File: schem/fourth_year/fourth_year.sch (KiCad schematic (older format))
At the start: 108 parts, among them P1 F Type, P10 BNC, P11 CONNECTOR, P12 CONNECTOR, P2 SAW, P3 CONNECTOR, P4 DC JACK, P5 CONNECTOR, P6 CONN_6, P7 CONN_1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

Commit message: More PCB work
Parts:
- removed P7: CONN_1, THROUGH HOLE CONN, symbol CONN_1
- removed P8: CONN_1, ~, symbol CONN_1
- added C54, C55, C56: 3uF, ~, symbol C
- added P7: BNC, ~, symbol BNC
- added T2: TRANSFO4, ~, symbol TRANSFO4
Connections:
- wire segments 441 -> 460
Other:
- note added: "I've put the + signal into the - input\nfor board routing convenience."

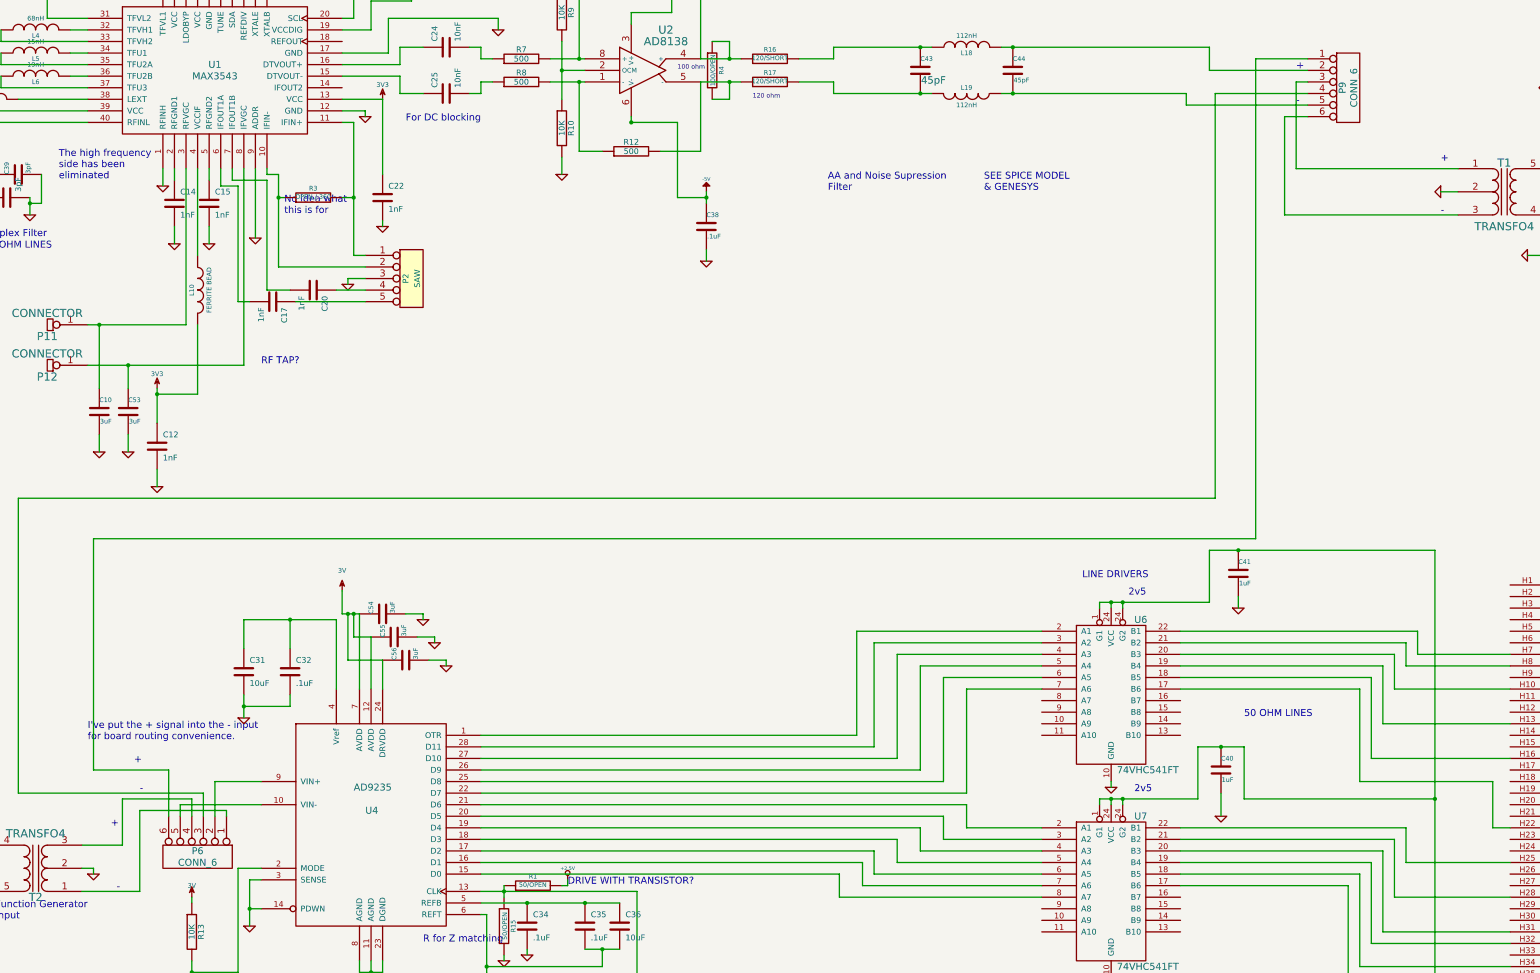
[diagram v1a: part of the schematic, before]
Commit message: Started routing ADC
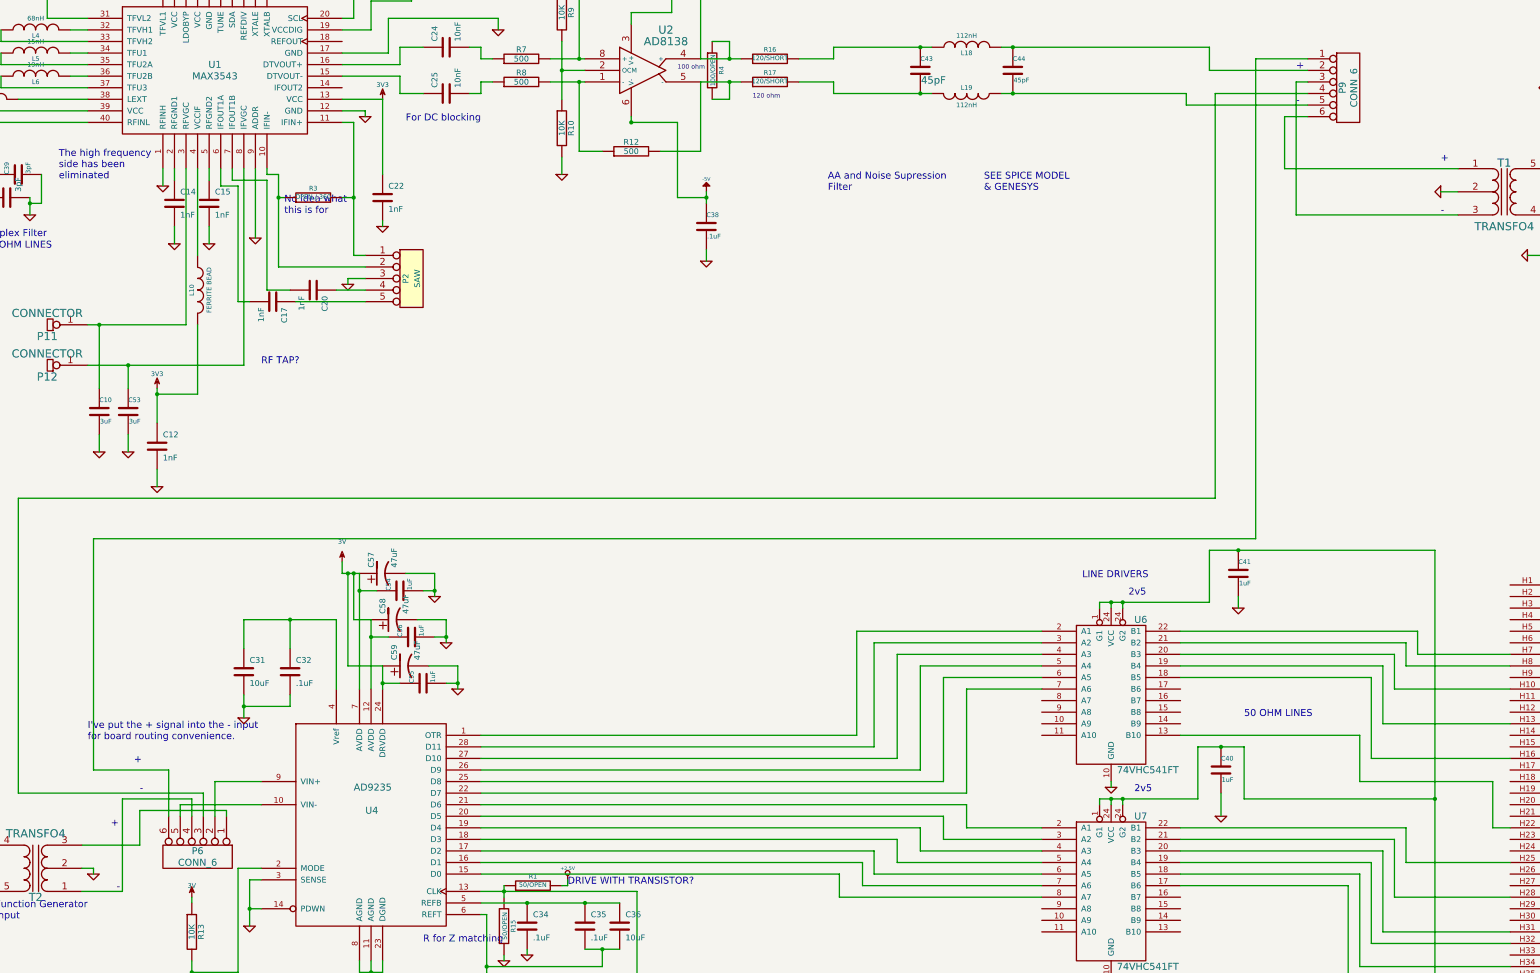
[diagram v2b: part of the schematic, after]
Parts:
- added C57, C58, C59: 47uF, ~, symbol CP1
- C54, C55, C56: value 3uF -> 1uF
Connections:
- wire segments 460 -> 466
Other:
- moved on the sheet: C54, C55, C56
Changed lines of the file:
@@
 Sheet 1 1
 Title ""
-Date "8 jan 2015"
+Date "9 jan 2015"
 Rev ""
 Comp ""
@@
 L 3V #PWR013
 U 1 1 54847F25
-P 4750 9850
-F 0 "#PWR013" H 4750 9950 40  0001 C CNN
-F 1 "3V" H 4750 10025 40  0000 C CNN
-F 2 "" H 4750 9850 60  0001 C CNN
-F 3 "" H 4750 9850 60  0001 C CNN
-	1    4750 9850
+P 4750 9600
+F 0 "#PWR013" H 4750 9700 40  0001 C CNN
+F 1 "3V" H 4750 9775 40  0000 C CNN
+F 2 "" H 4750 9600 60  0001 C CNN
+F 3 "" H 4750 9600 60  0001 C CNN
+	1    4750 9600
 	1    0    0    -1
 $EndComp
@@
 L C C55
 U 1 1 54AF12A6
-P 5200 10250
-F 0 "C55" H 5200 10350 40  0000 L CNN
-F 1 "3uF" H 5206 10165 40  0000 L CNN
-F 2 "~" H 5238 10100 30  0000 C CNN
-F 3 "~" H 5200 10250 60  0000 C CNN
-	1    5200 10250
+P 5450 10650
+F 0 "C55" H 5450 10750 40  0000 L CNN
+F 1 "1uF" H 5456 10565 40  0000 L CNN
+F 2 "~" H 5488 10500 30  0000 C CNN
+F 3 "~" H 5450 10650 60  0000 C CNN
+	1    5450 10650
 	0    -1   -1   0
 $EndComp
@@
 L C C54
 U 1 1 54AF12B5
-P 5100 10050
-F 0 "C54" H 5100 10150 40  0000 L CNN
-F 1 "3uF" H 5106 9965 40  0000 L CNN
-F 2 "~" H 5138 9900 30  0000 C CNN
-F 3 "~" H 5100 10050 60  0000 C CNN
-	1    5100 10050
+P 5250 9850
+F 0 "C54" H 5250 9950 40  0000 L CNN
+F 1 "1uF" H 5256 9765 40  0000 L CNN
+F 2 "~" H 5288 9700 30  0000 C CNN
+F 3 "~" H 5250 9850 60  0000 C CNN
+	1    5250 9850
 	0    -1   -1   0
 $EndComp
@@
 L C C56
 U 1 1 54AF258D
-P 5300 10450
-F 0 "C56" H 5300 10550 40  0000 L CNN
-F 1 "3uF" H 5306 10365 40  0000 L CNN
-F 2 "~" H 5338 10300 30  0000 C CNN
-F 3 "~" H 5300 10450 60  0000 C CNN
-	1    5300 10450
+P 5350 10250
+F 0 "C56" H 5350 10350 40  0000 L CNN
+F 1 "1uF" H 5356 10165 40  0000 L CNN
+F 2 "~" H 5388 10100 30  0000 C CNN
+F 3 "~" H 5350 10250 60  0000 C CNN
+	1    5350 10250
 	0    -1   -1   0
 $EndComp
+Text Notes 2550 11150 0    60   ~ 0
+I've put the + signal into the - input\nfor board routing convenience.
+$Comp
+L CP1 C58
+U 1 1 54B05B86
+P 5200 10100
+F 0 "C58" H 5250 10200 50  0000 L CNN
+F 1 "47uF" H 5250 10000 50  0000 L CNN
+F 2 "~" H 5200 10100 60  0000 C CNN
+F 3 "~" H 5200 10100 60  0000 C CNN
+	1    5200 10100
+	0    -1   -1   0
+$EndComp
+$Comp
+L CP1 C57
+U 1 1 54B05B93
+P 5100 9700
+F 0 "C57" H 5150 9800 50  0000 L CNN
+F 1 "47uF" H 5150 9600 50  0000 L CNN
+F 2 "~" H 5100 9700 60  0000 C CNN
+F 3 "~" H 5100 9700 60  0000 C CNN
+	1    5100 9700
+	0    -1   -1   0
+$EndComp
+$Comp
+L CP1 C59
+U 1 1 54B05B99
+P 5300 10500
+F 0 "C59" H 5350 10600 50  0000 L CNN
+F 1 "47uF" H 5350 10400 50  0000 L CNN
+F 2 "~" H 5300 10500 60  0000 C CNN
+F 3 "~" H 5300 10500 60  0000 C CNN
+	1    5300 10500
+	0    -1   -1   0
+$EndComp
+$Comp
+L GND #PWR086
+U 1 1 54B0765F
+P 5750 10700
+F 0 "#PWR086" H 5750 10700 30  0001 C CNN
+F 1 "GND" H 5750 10630 30  0001 C CNN
+F 2 "" H 5750 10700 60  0000 C CNN
+F 3 "" H 5750 10700 60  0000 C CNN
+	1    5750 10700
+	1    0    0    -1
+$EndComp
+$Comp
+L GND #PWR087
+U 1 1 54B0766C
+P 5650 10300
+F 0 "#PWR087" H 5650 10300 30  0001 C CNN
+F 1 "GND" H 5650 10230 30  0001 C CNN
+F 2 "" H 5650 10300 60  0000 C CNN
+F 3 "" H 5650 10300 60  0000 C CNN
+	1    5650 10300
+	1    0    0    -1
+$EndComp
+$Comp
+L GND #PWR088
+U 1 1 54B07672
+P 5550 9900
+F 0 "#PWR088" H 5550 9900 30  0001 C CNN
+F 1 "GND" H 5550 9830 30  0001 C CNN
+F 2 "" H 5550 9900 60  0000 C CNN
+F 3 "" H 5550 9900 60  0000 C CNN
+	1    5550 9900
+	1    0    0    -1
+$EndComp
 Wire Wire Line
 	4000 6800 4000 6200
@@
 	15200 6200 15500 6200
 Wire Wire Line
-	14400 6600 12900 6600
-Wire Wire Line
-	13000 6200 13000 5450
-Wire Wire Line
-	14400 6200 13000 6200
+	13000 5450 13000 6600
 Wire Wire Line
 	15350 6100 15350 6200
@@
 	13000 5450 13100 5450
 Wire Wire Line
-	12900 6600 12900 5750
-Wire Wire Line
 	12900 5750 13100 5750
 Wire Wire Line
@@
 	14700 11500 13550 11500
 Wire Wire Line
-	13550 11500 13550 10700
-Wire Wire Line
-	13550 10700 12000 10700
+	13550 11500 13550 11100
 Wire Wire Line
 	13950 12200 13950 11900
@@
 	2600 12250 2600 12300
 Wire Wire Line
-	2500 12050 2850 12050
-Wire Wire Line
-	2850 12050 2850 11650
+	2850 11650 2850 12450
 Wire Wire Line
 	2850 11650 3450 11650
@@
 	3450 11650 3450 11800
 Wire Wire Line
-	2500 12450 3000 12450
-Wire Wire Line
-	3000 12450 3000 11750
-Wire Wire Line
 	3000 11750 3750 11750
 Wire Wire Line
@@
 	1450 12050 1700 12050
 Wire Wire Line
-	4750 10050 4900 10050
+	3650 11500 4050 11500
 Wire Wire Line
-	4750 10050 4750 9850
+	3350 11800 3350 11700
 Wire Wire Line
-	4900 10050 4900 10700
+	3350 11700 4050 11700
 Wire Wire Line
-	5000 10250 5000 10700
+	12900 5750 12900 6200
 Wire Wire Line
-	5100 10450 5100 10700
+	12900 6200 14400 6200
 Wire Wire Line
-	4850 10050 4850 10250
+	13000 6600 14400 6600
 Wire Wire Line
-	4850 10250 5000 10250
-Connection ~ 4850 10050
+	2850 12450 2500 12450
 Wire Wire Line
-	4800 10050 4800 10450
+	2500 12050 3000 12050
 Wire Wire Line
-	4800 10450 5100 10450
-Connection ~ 4800 10050
-$Comp
-L GND #PWR086
-U 1 1 54AF4903
-P 5450 10100
-F 0 "#PWR086" H 5450 10100 30  0001 C CNN
-F 1 "GND" H 5450 10030 30  0001 C CNN
-F 2 "" H 5450 10100 60  0000 C CNN
-F 3 "" H 5450 10100 60  0000 C CNN
-	1    5450 10100
-	1    0    0    -1
-$EndComp
-$Comp
-L GND #PWR087
-U 1 1 54AF4910
-P 5550 10300
-F 0 "#PWR087" H 5550 10300 30  0001 C CNN
-F 1 "GND" H 5550 10230 30  0001 C CNN
-F 2 "" H 5550 10300 60  0000 C CNN
-F 3 "" H 5550 10300 60  0000 C CNN
-	1    5550 10300
-	1    0    0    -1
-$EndComp
-$Comp
-L GND #PWR088
-U 1 1 54AF491C
-P 5650 10500
-F 0 "#PWR088" H 5650 10500 30  0001 C CNN
-F 1 "GND" H 5650 10430 30  0001 C CNN
-F 2 "" H 5650 10500 60  0000 C CNN
-F 3 "" H 5650 10500 60  0000 C CNN
-	1    5650 10500
-	1    0    0    -1
-$EndComp
+	3000 12050 3000 11750
 Wire Wire Line
-	5300 10050 5450 10050
+	4750 9600 4750 9700
 Wire Wire Line
-	5450 10050 5450 10100
+	4750 9700 4900 9700
 Wire Wire Line
-	5400 10250 5550 10250
+	4900 9700 4900 10700
 Wire Wire Line
-	5550 10250 5550 10300
+	5050 9850 4900 9850
+Connection ~ 4900 9850
 Wire Wire Line
-	5500 10450 5650 10450
+	4850 9700 4850 10100
 Wire Wire Line
-	5650 10450 5650 10500
+	4850 10100 5000 10100
+Connection ~ 4850 9700
 Wire Wire Line
-	3650 11500 4050 11500
+	4800 9700 4800 10500
 Wire Wire Line
-	3350 11800 3350 11700
+	4800 10500 5100 10500
+Connection ~ 4800 9700
 Wire Wire Line
-	3350 11700 4050 11700
-Text Notes 2550 11150 0    60   ~ 0
-I've put the + signal into the - input\nfor board routing convenience.
+	5000 10100 5000 10700
+Wire Wire Line
+	5150 10250 5000 10250
+Connection ~ 5000 10250
+Wire Wire Line
+	5100 10500 5100 10700
+Wire Wire Line
+	5250 10650 5100 10650
+Connection ~ 5100 10650
+Wire Wire Line
+	5300 9700 5550 9700
+Wire Wire Line
+	5550 9700 5550 9900
+Wire Wire Line
+	5450 9850 5550 9850
+Connection ~ 5550 9850
+Wire Wire Line
+	5400 10100 5650 10100
+Wire Wire Line
+	5650 10100 5650 10300
+Wire Wire Line
+	5550 10250 5650 10250
+Connection ~ 5650 10250
+Wire Wire Line
+	5500 10500 5750 10500
+Wire Wire Line
+	5750 10500 5750 10700
+Wire Wire Line
+	5650 10650 5750 10650
+Connection ~ 5750 10650
+Wire Wire Line
+	13550 11100 12000 11100
 $EndSCHEMATC

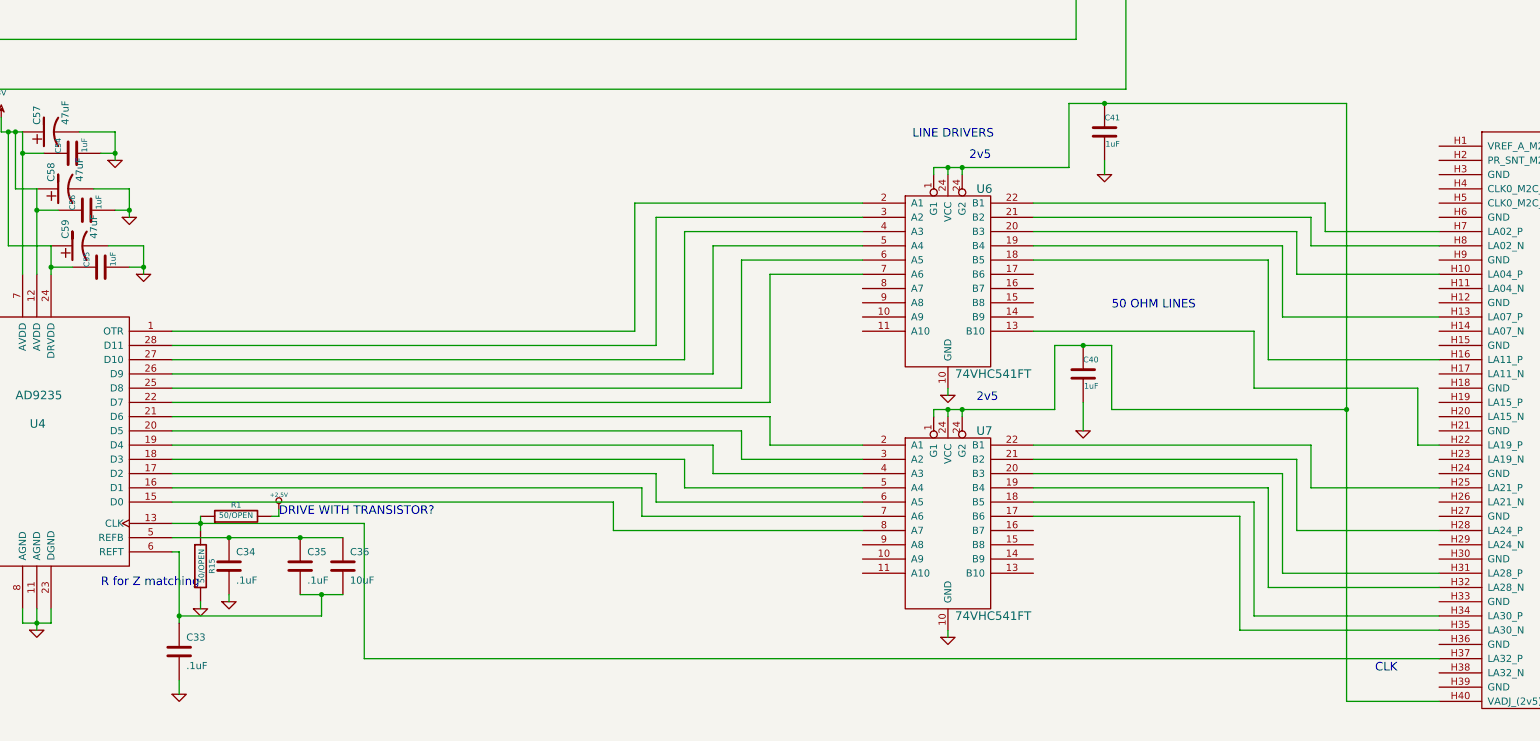
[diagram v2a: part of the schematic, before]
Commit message: Routed line drivers
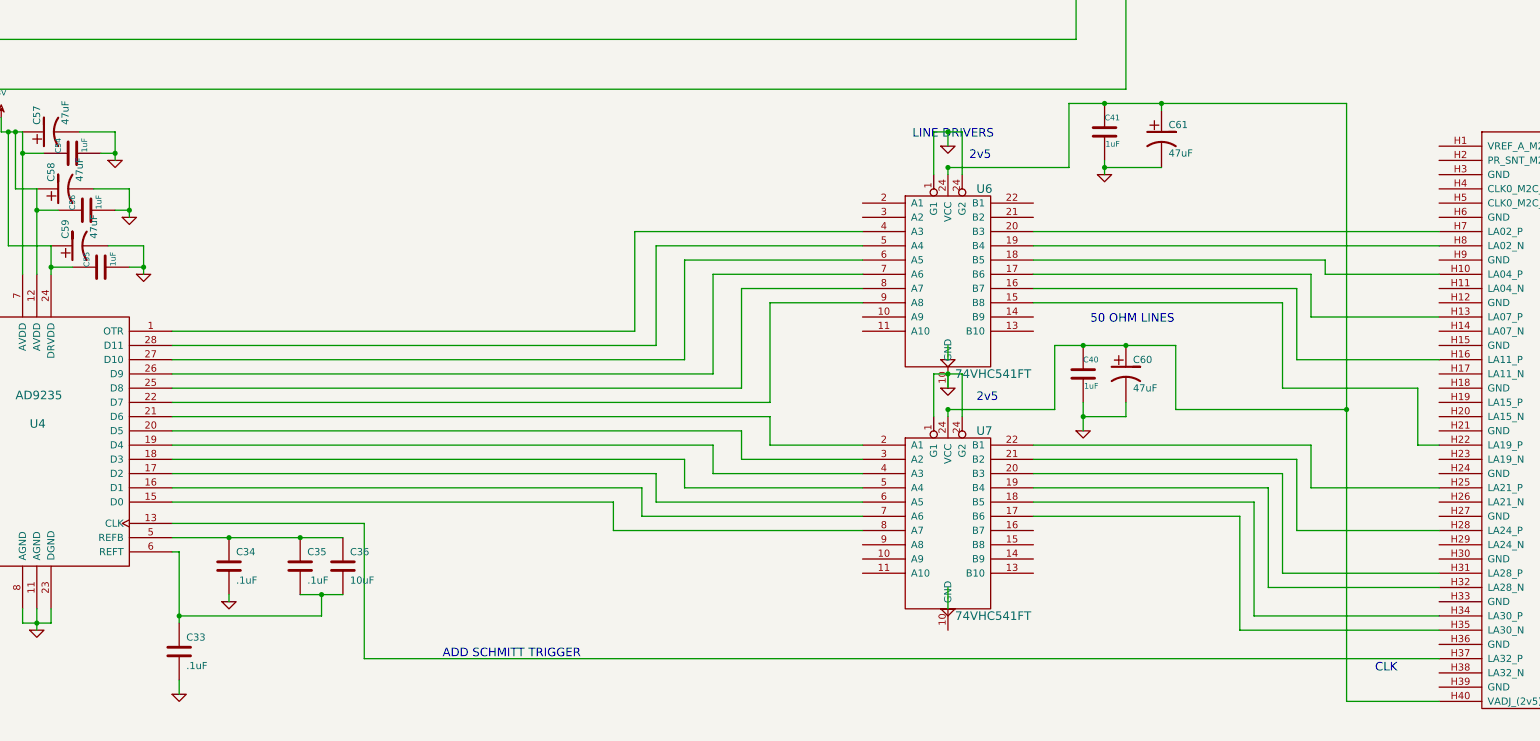
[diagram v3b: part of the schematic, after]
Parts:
- removed R1, R15: 50/OPEN, 3.20mm x 1.60mm, symbol R
- added C60, C61: 47uF, ~, symbol CP1
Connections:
- net labels removed: +2,5V
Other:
- note added: "ADD SCHMITT TRIGGER"
- note removed: "DRIVE WITH TRANSISTOR?"
- note removed: "R for Z matching"

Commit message: PCB routing done.  Doing some optimization and copper fills
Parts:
- removed T2: TRANSFO4, ~, symbol TRANSFO4
- added P8: BNC, ~, symbol BNC
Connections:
- wire segments 466 -> 573
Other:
- note added: "Function Generator\nInputs"
- note removed: "Function Generator\nInput"
- moved on the sheet: P7

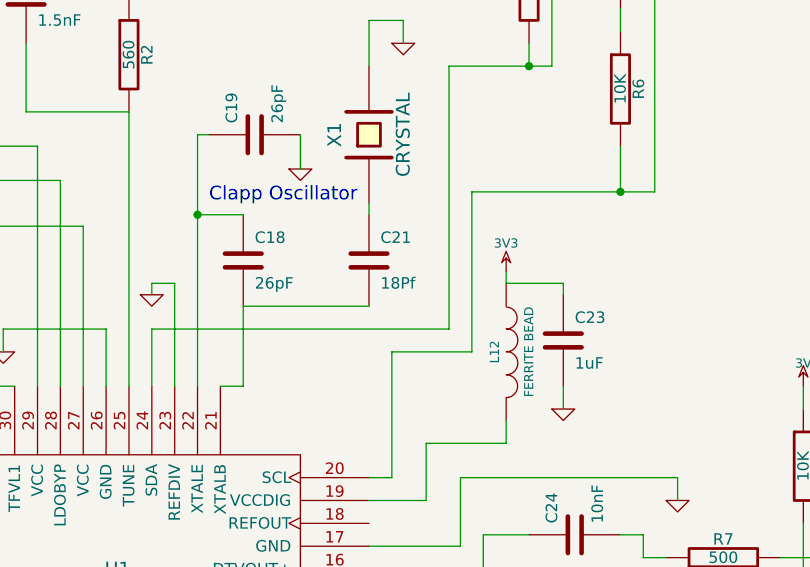
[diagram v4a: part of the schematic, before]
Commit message: Polishing PCB layout.  Ground planes, copper pours, vias etc... Checking correctness
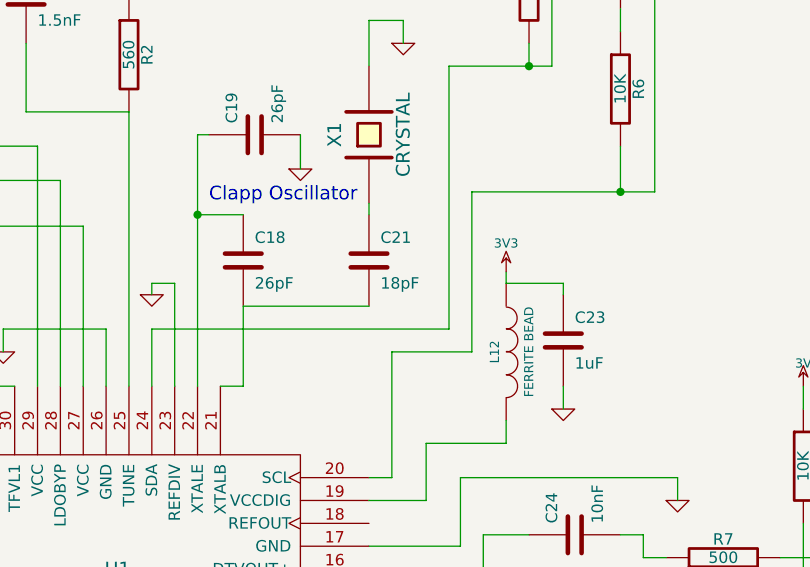
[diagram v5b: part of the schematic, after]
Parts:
- C21: value 18Pf -> 18pF

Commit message: PCB finalized, order has been placed
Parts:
- added L1, L7: OPEN, ~, symbol INDUCTOR
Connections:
- wire segments 573 -> 578
